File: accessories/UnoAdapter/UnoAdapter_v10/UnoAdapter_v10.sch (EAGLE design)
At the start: 13 parts, among them IC1 7805, X1 DC21MMX

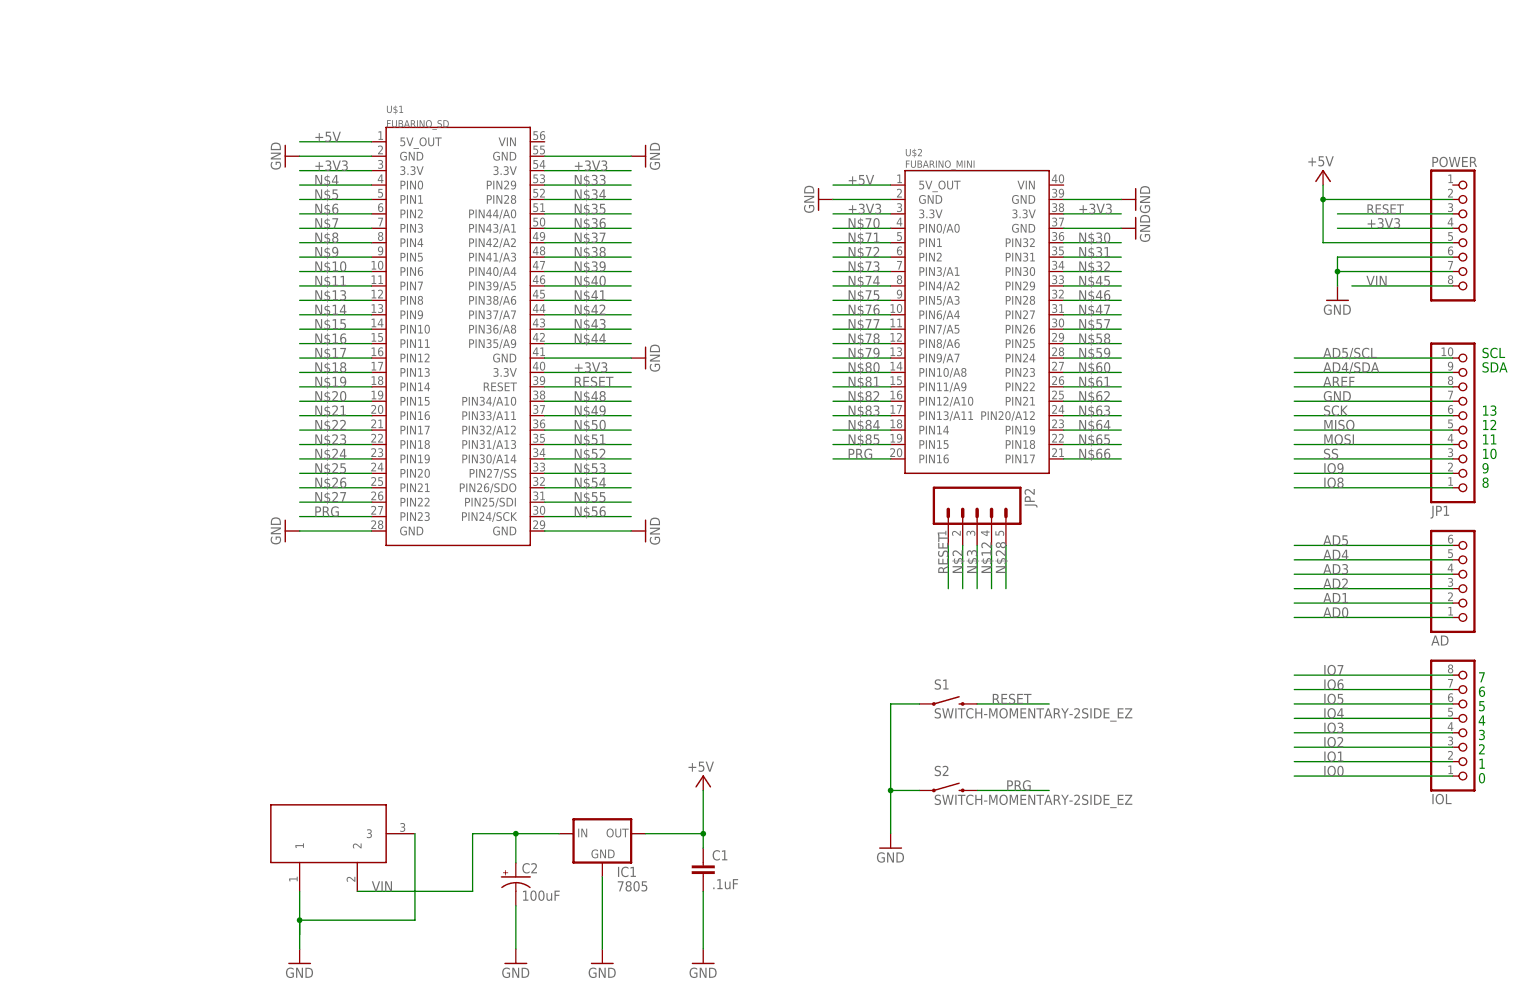
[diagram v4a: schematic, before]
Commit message: Update to UnoAdapter - still not done yet. Added Fubarino Mini v1.6 files (brought MCLR out to side pin)
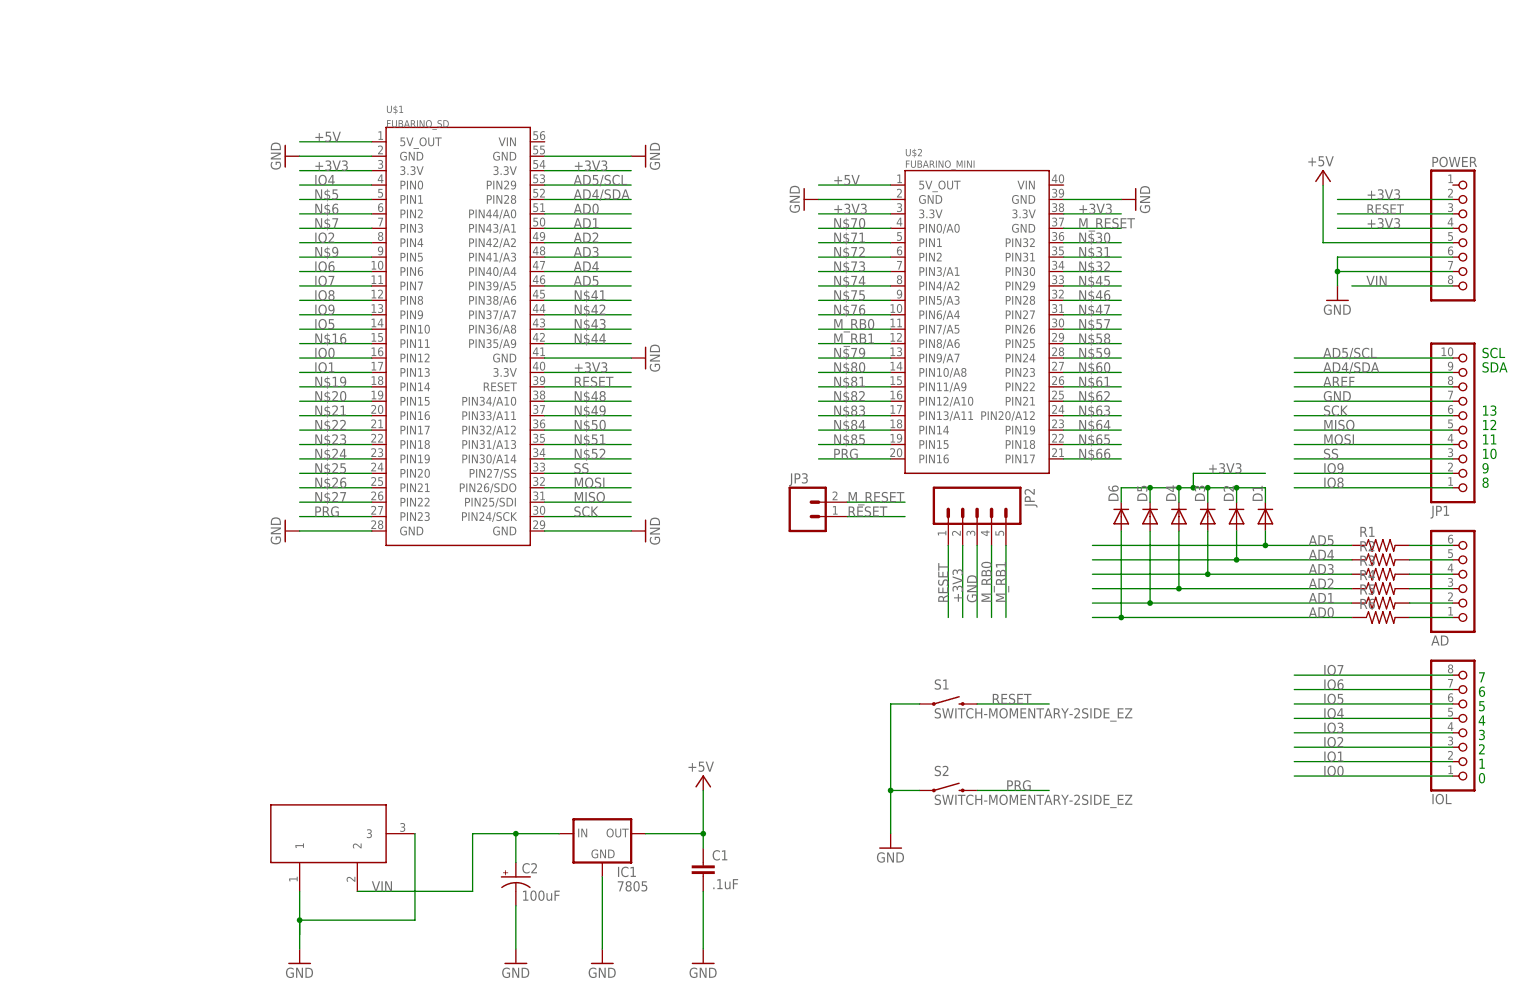
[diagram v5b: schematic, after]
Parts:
- added D1, D2, D3, D4, D5, D6: (no value), SparkFun-DiscreteSemi:DIODE1N4148
- added JP3: (no value), SparkFun-Connectors:M02PTH
- added R1, R2, R3, R4, R5, R6: (no value), SparkFun-Passives:RESISTORAXIAL-0.3
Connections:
- removed net N$10: U$1.PIN6
- removed net N$11: U$1.PIN7
- removed net N$12: JP2.4
- removed net N$13: U$1.PIN8
- removed net N$14: U$1.PIN9
- removed net N$15: U$1.PIN10
- removed net N$17: U$1.PIN12
- removed net N$18: U$1.PIN13
- removed net N$2: JP2.2
- removed net N$28: JP2.5
- removed net N$3: JP2.3
- removed net N$33: U$1.PIN29
- removed net N$34: U$1.PIN28
- removed net N$35: U$1.PIN44/A0
- removed net N$36: U$1.PIN43/A1
- removed net N$37: U$1.PIN42/A2
- removed net N$38: U$1.PIN41/A3
- removed net N$39: U$1.PIN40/A4
- removed net N$4: U$1.PIN0
- removed net N$40: U$1.PIN39/A5
- removed net N$53: U$1.PIN27/SS
- removed net N$54: U$1.PIN26/SDO
- removed net N$55: U$1.PIN25/SDI
- removed net N$56: U$1.PIN24/SCK
- removed net N$77: U$2.PIN7/A5
- removed net N$78: U$2.PIN8/A6
- removed net N$8: U$1.PIN4
- new net $12: AD.6, R1.2
- new net $13: AD.5, R2.2
- new net $14: AD.4, R3.2
- new net $15: AD.3, R4.2
- new net $16: AD.2, R5.2
- new net $17: AD.1, R6.2
- new net M_RB0: JP2.4, U$2.PIN7/A5
- new net M_RB1: JP2.5, U$2.PIN8/A6
- new net M_RESET: JP3.2, U$2.GND@4
- net +3V3: now also D1.C, D2.C, D3.C, D4.C, D5.C, D6.C, JP2.2, POWER.2
- net +5V: no longer POWER.2
- net AD0: now also D6.A, R6.1, U$1.PIN44/A0; no longer AD.1
- net AD1: now also D5.A, R5.1, U$1.PIN43/A1; no longer AD.2
- net AD2: now also D4.A, R4.1, U$1.PIN42/A2; no longer AD.3
- net AD3: now also D3.A, R3.1, U$1.PIN41/A3; no longer AD.4
- net AD4: now also D2.A, R2.1, U$1.PIN40/A4; no longer AD.5
- net AD4/SDA: now also U$1.PIN28
- net AD5: now also D1.A, R1.1, U$1.PIN39/A5; no longer AD.6
- net AD5/SCL: now also U$1.PIN29
- net GND: now also JP2.3; no longer U$2.GND@4
- net IO0: now also U$1.PIN12
- net IO1: now also U$1.PIN13
- net IO2: now also U$1.PIN4
- net IO4: now also U$1.PIN0
- net IO5: now also U$1.PIN10
- net IO6: now also U$1.PIN6
- net IO7: now also U$1.PIN7
- net IO8: now also U$1.PIN8
- net IO9: now also U$1.PIN9
- net MISO: now also U$1.PIN25/SDI
- net MOSI: now also U$1.PIN26/SDO
- net RESET: now also JP3.1
- net SCK: now also U$1.PIN24/SCK
- net SS: now also U$1.PIN27/SS
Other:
- note added: "RX<-"
- note added: "TX->"

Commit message: First rough draft of schematic done, first super crappy routing done.
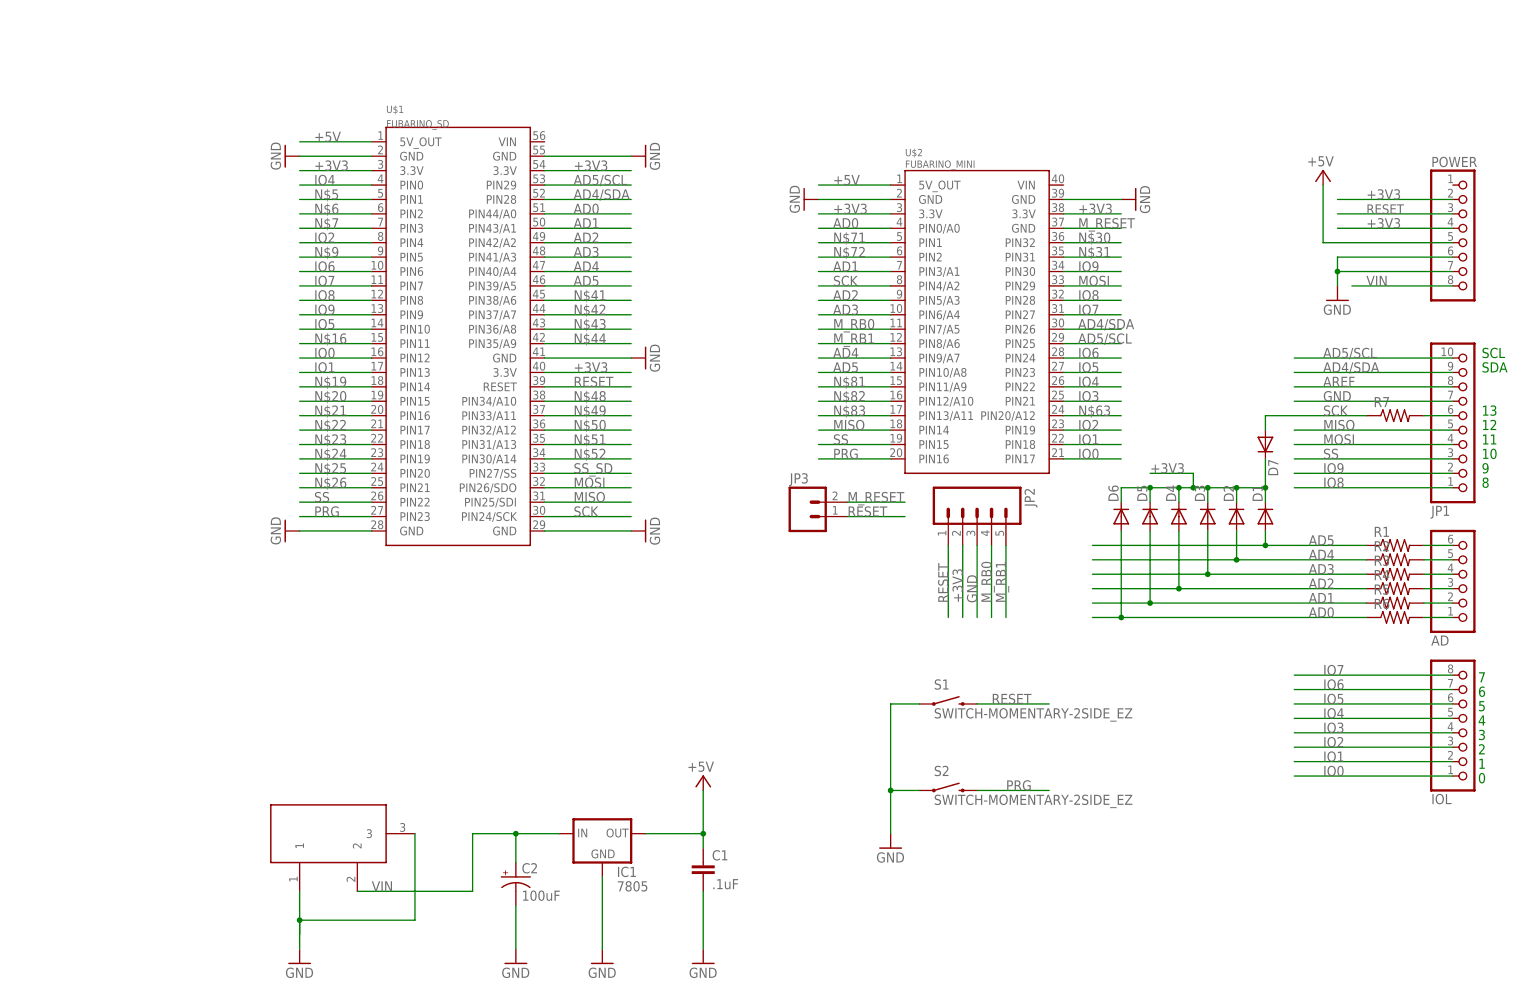
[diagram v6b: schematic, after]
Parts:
- added D7: (no value), SparkFun-DiscreteSemi:DIODE1N4148
- added R7: (no value), SparkFun-Passives:RESISTORAXIAL-0.3
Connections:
- removed net N$27: U$1.PIN22
- removed net N$32: U$2.PIN30
- removed net N$45: U$2.PIN29
- removed net N$46: U$2.PIN28
- removed net N$47: U$2.PIN27
- removed net N$57: U$2.PIN26
- removed net N$58: U$2.PIN25
- removed net N$59: U$2.PIN24
- removed net N$60: U$2.PIN23
- removed net N$61: U$2.PIN22
- removed net N$62: U$2.PIN21
- removed net N$64: U$2.PIN19
- removed net N$65: U$2.PIN18
- removed net N$66: U$2.PIN17
- removed net N$70: U$2.PIN0/A0
- removed net N$73: U$2.PIN3/A1
- removed net N$74: U$2.PIN4/A2
- removed net N$75: U$2.PIN5/A3
- removed net N$76: U$2.PIN6/A4
- removed net N$79: U$2.PIN9/A7
- removed net N$80: U$2.PIN10/A8
- removed net N$84: U$2.PIN14
- removed net N$85: U$2.PIN15
- new net $123: JP1.6, R7.2
- new net SS_SD: U$1.PIN27/SS
- net +3V3: now also D7.C
- net AD0: now also U$2.PIN0/A0
- net AD1: now also U$2.PIN3/A1
- net AD2: now also U$2.PIN5/A3
- net AD3: now also U$2.PIN6/A4
- net AD4: now also U$2.PIN9/A7
- net AD4/SDA: now also U$2.PIN26
- net AD5: now also U$2.PIN10/A8
- net AD5/SCL: now also U$2.PIN25
- net IO0: now also U$2.PIN17
- net IO1: now also U$2.PIN18
- net IO2: now also U$2.PIN19
- net IO3: now also U$2.PIN21
- net IO4: now also U$2.PIN22
- net IO5: now also U$2.PIN23
- net IO6: now also U$2.PIN24
- net IO7: now also U$2.PIN27
- net IO8: now also U$2.PIN28
- net IO9: now also U$2.PIN30
- net MISO: now also U$2.PIN14
- net MOSI: now also U$2.PIN29
- net SCK: now also D7.A, R7.1, U$2.PIN4/A2; no longer JP1.6
- net SS: now also U$1.PIN22, U$2.PIN15; no longer U$1.PIN27/SS
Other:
- note added: "Version T1"
- moved on the sheet: R1, R2, R3, R4, R5, R6
